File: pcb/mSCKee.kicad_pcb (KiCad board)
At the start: 2 copper layers, 184 parts, among them IC1 PCA9956BTWY, IC2 PCA9956BTWY, J1 USB_C_Receptacle_USB2.0_14P, J2 4P4C, J3 4P4C, SW1 SW_Push_45deg, SW10 SW_Push_45deg, SW11 SW_Push_45deg, SW12 SW_Push_45deg, SW13 SW_Push_45deg, SW14 SW_Push_45deg, SW15 SW_Push_45deg, SW16 SW_Push_45deg, SW17 SW_Push_45deg, SW18 SW_Push_45deg, SW19 SW_Push, SW2 SW_Push_45deg, SW20 SW_Push, SW21 SW_SP3T, SW22 SW_Push_45deg, SW23 SW_Push_45deg, SW24 SW_Push_45deg, SW25 SW_Push_45deg, SW26 SW_Push_45deg, SW27 SW_Push_45deg, SW28 SW_Push_45deg, SW29 SW_Push_45deg, SW3 SW_Push_45deg, SW30 SW_Push_45deg, SW31 SW_Push_45deg, SW32 SW_Push_45deg, SW33 SW_Push_45deg, SW34 SW_Push_45deg, SW35 SW_Push_45deg, SW36 SW_Push_45deg, SW37 SW_Push_45deg, SW38 SW_Push_45deg, SW39 SW_Push_45deg, SW4 SW_Push_45deg, SW5 SW_Push_45deg, SW6 SW_Push_45deg, SW7 SW_Push_45deg, SW8 SW_Push_45deg, SW9 SW_Push_45deg, U1 W25Q128JVSIQ, U2 RP2040, U3 NCP1117LPST33T3G, U4 OPT3001DNPR, U5 NCP1117LPST33T3G, U6 MCP23017T-E/ML, U7 OPT3001DNPR, Y1 ABM8-272-T3

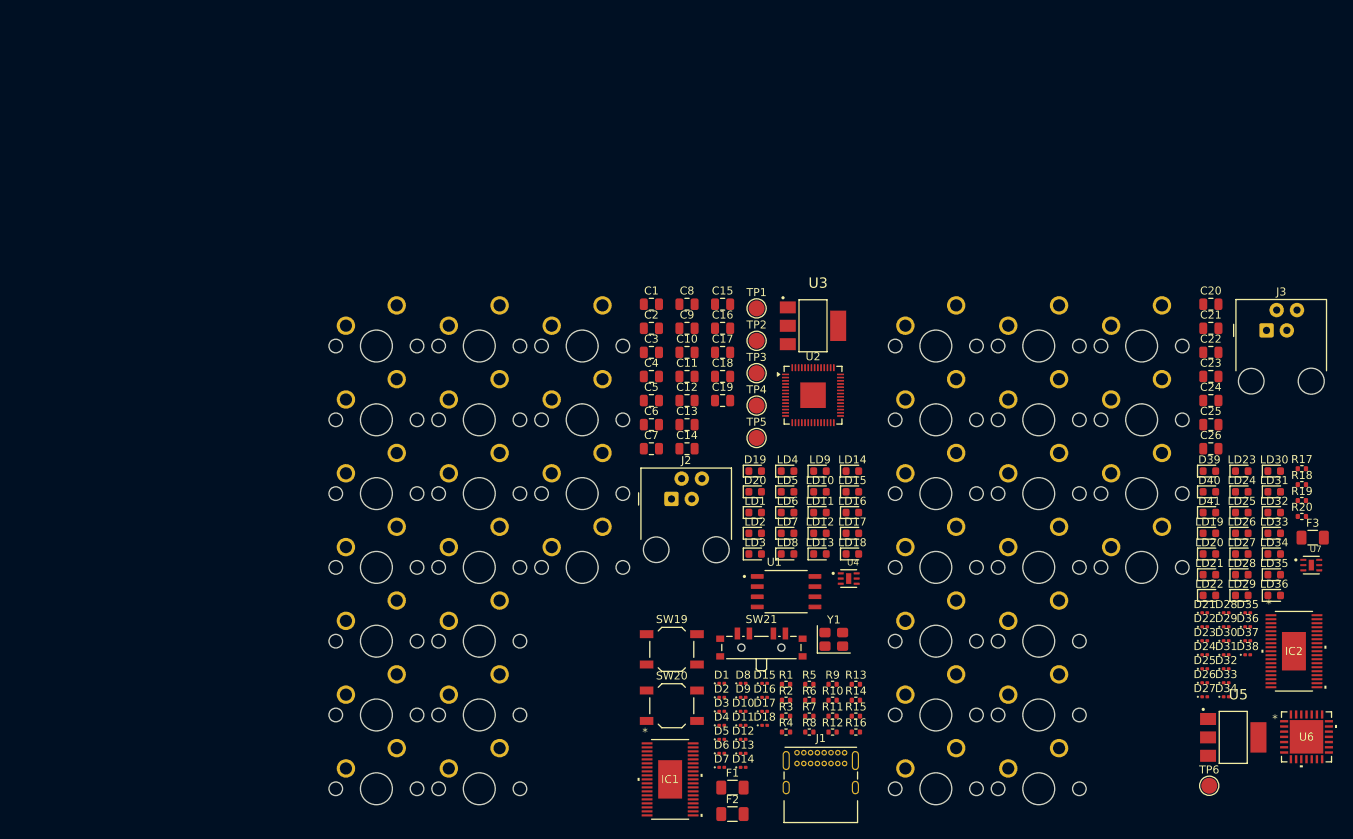
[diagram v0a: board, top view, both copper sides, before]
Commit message: fix: Proper USB-C receptacle symbol
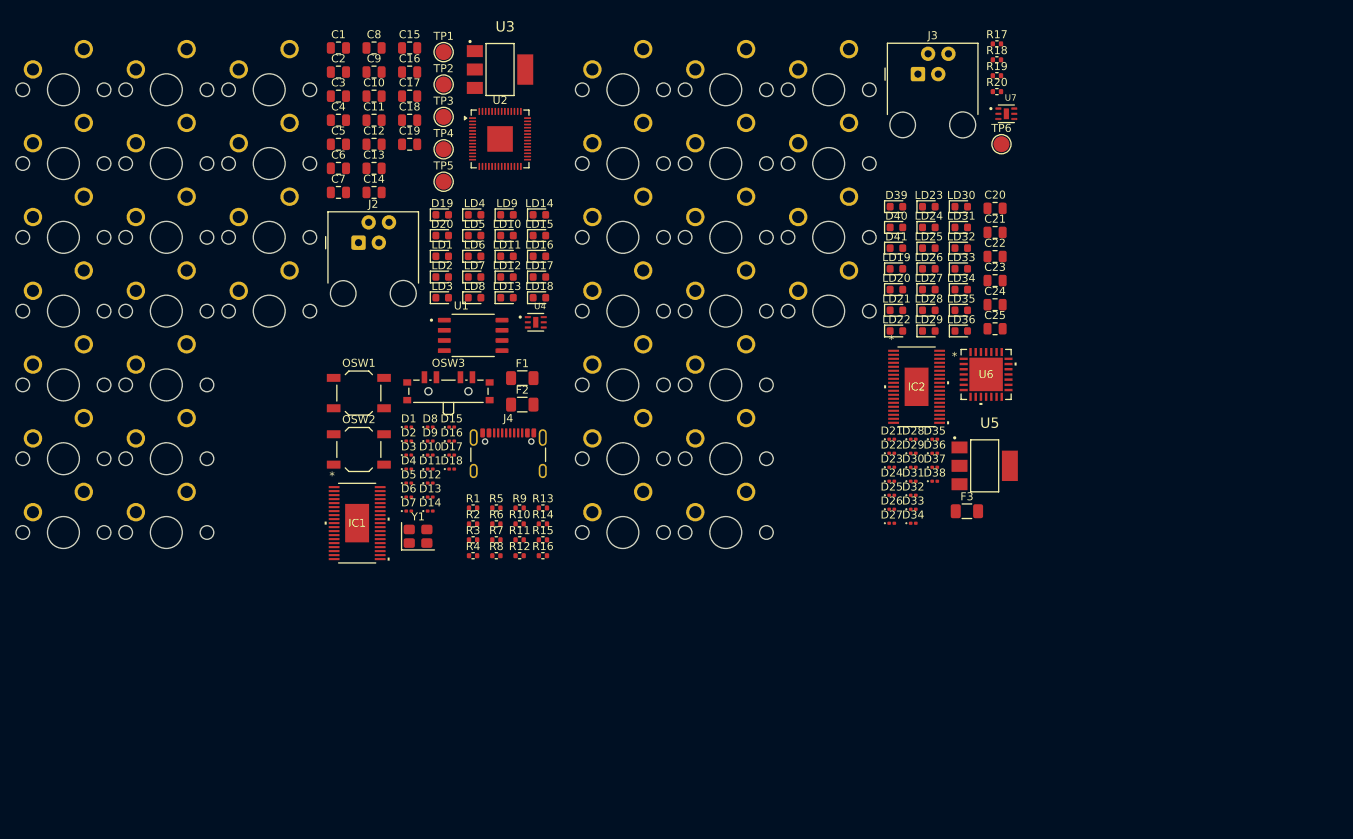
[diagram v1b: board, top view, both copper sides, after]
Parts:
- removed C26: 10u, Capacitor_SMD:C_0805_2012Metric
- removed J1: USB_C_Receptacle_USB2.0_14P, Connector_USB:USB_C_Receptacle_GCT_USB4085
- removed SW37, SW38, SW39: SW_Push_45deg, ai03-MX_V2:MX-Solderable-1U
- added J4: USB_C_Receptacle_USB2.0_16P, Connector_USB:USB_C_Receptacle_GCT_USB4105-xx-A_16P_TopMnt_Horizontal, F.Cu at (194.8, 137.9)
- added OSW1: SW_Push, Button_Switch_SMD:SW_SPST_TL3342, F.Cu at (176.1, 129.2)
- added OSW2: SW_Push, Button_Switch_SMD:SW_SPST_TL3342, F.Cu at (176.1, 136.3)
- added OSW3: SW_SP3T, Button_Switch_SMD:SW_SP3T_PCM13, F.Cu at (187.3, 128.7)
- C20: value 20u -> 10u
- C22: value 10u -> 100n
- C25: value 100n -> 10u
- R13: value R -> 10k
- R15: value 10k -> R
- SW19, SW20: value SW_Push -> SW_Push_45deg; footprint Button_Switch_SMD:SW_SPST_TL3342 -> ai03-MX_V2:MX-Solderable-1U
- SW21: value SW_SP3T -> SW_Push_45deg; footprint Button_Switch_SMD:SW_SP3T_PCM13 -> ai03-MX_V2:MX-Solderable-1U
- moved TP6 84.3 mm to (256.4, 98.1)
- moved SW27 73.8 mm to (222.0, 100.5)
- moved SW26 73.8 mm to (222.0, 91.3)
- moved SW28 73.8 mm to (222.0, 109.8)
- moved SW34 73.8 mm to (234.8, 100.5)
- moved SW33 73.8 mm to (234.8, 91.3)
- moved SW35 73.8 mm to (234.8, 109.8)
- moved SW19 70.2 mm to (209.1, 91.3)
- moved U7 68.1 mm to (257.0, 94.3)
- moved SW20 68.0 mm to (209.1, 100.5)
- moved R18 65.4 mm to (255.8, 87.6)
- moved R17 65.4 mm to (255.8, 85.6)
- moved R20 65.4 mm to (255.8, 91.5)
- moved R19 65.4 mm to (255.8, 89.6)
- moved U6 60.5 mm to (254.5, 126.9)
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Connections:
- net GPIO0 renamed I2C_D_R
- net GPIO1 renamed I2C_CLK_R
- net GPIO2 renamed I2C_D
- net GPIO3 renamed I2C_CLK
- net GPIO5 renamed STATUS2
- C21 pad 1: +5V_R -> +3V3_R
- C22 pad 1: +3V3_R -> unconnected-(C22-Pad1)
- C22 pad 2: unconnected-(C22-Pad2) -> +3V3_R
- C24 pad 1: unconnected-(C24-Pad1) -> +3V3_R
- C24 pad 2: +3V3_R -> unconnected-(C24-Pad2)
- C25 pad 1: +3V3_R -> +5V_R
- R13 pad 1: GPIO4 -> OE_ENABLE
- R13 pad 2: Net-(D19-A) -> +3V3
- R14 pad 1: OE_ENABLE -> +3V3
- R14 pad 2: +3V3 -> Net-(IC1-RESET)
- R15 pad 1: +3V3 -> STATUS1
- R15 pad 2: Net-(IC1-RESET) -> Net-(D19-A)
- R9 pad 2: Net-(R9-Pad2) -> Net-(OSW1-Pad2)
- SW19 pad 1: GND -> COL1R
- SW19 pad 2: Net-(R9-Pad2) -> Net-(D21-A)
- SW20 pad 1: GND -> COL2R
- SW20 pad 2: Net-(U2-RUN) -> Net-(D22-A)
- SW21 pad 1: GPIO6 -> COL3R
- SW21 pad 2: GPIO7 -> Net-(D23-A)
- SW22 pad 1: COL1R -> COL4R
- SW22 pad 2: Net-(D21-A) -> Net-(D24-A)
- SW23 pad 1: COL2R -> COL5R
- SW23 pad 2: Net-(D22-A) -> Net-(D25-A)
- SW24 pad 1: COL3R -> COL6R
- SW24 pad 2: Net-(D23-A) -> Net-(D26-A)
- SW25 pad 1: COL4R -> COL1R
- SW25 pad 2: Net-(D24-A) -> Net-(D27-A)
- SW26 pad 1: COL5R -> COL2R
- SW26 pad 2: Net-(D25-A) -> Net-(D28-A)
- SW27 pad 1: COL6R -> COL3R
- SW27 pad 2: Net-(D26-A) -> Net-(D29-A)
- SW28 pad 1: COL1R -> COL4R
- SW28 pad 2: Net-(D27-A) -> Net-(D30-A)
- SW29 pad 1: COL2R -> COL5R
- SW29 pad 2: Net-(D28-A) -> Net-(D31-A)
- SW30 pad 1: COL3R -> COL6R
- SW30 pad 2: Net-(D29-A) -> Net-(D32-A)
- SW31 pad 1: COL4R -> COL1R
- SW31 pad 2: Net-(D30-A) -> Net-(D33-A)
- SW32 pad 1: COL5R -> COL2R
- SW32 pad 2: Net-(D31-A) -> Net-(D34-A)
- SW33 pad 1: COL6R -> COL3R
- SW33 pad 2: Net-(D32-A) -> Net-(D35-A)
- SW34 pad 1: COL1R -> COL4R
- SW34 pad 2: Net-(D33-A) -> Net-(D36-A)
- SW35 pad 1: COL2R -> COL5R
- SW35 pad 2: Net-(D34-A) -> Net-(D37-A)
- SW36 pad 1: COL3R -> COL6R
- SW36 pad 2: Net-(D35-A) -> Net-(D38-A)
- U2 pad 11: GPIO8 -> BL_DIM_3
- U2 pad 6: GPIO4 -> STATUS1
- U2 pad 8: GPIO6 -> BL_DIM_1
- U2 pad 9: GPIO7 -> BL_DIM_2

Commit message: fix: Fix thumb cluster key splay & Correctly align keys to outline in PCB layout
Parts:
- D1, D10, D11, D12, D13, D14, D15, D16, D17, D18, D2, D21, D22, D23, D24, D25, D26, D27, D28, D29, D3, D30, D31, D32, D33, D34, D35, D36, D37, D38, D4, D5, D6, D7, D8, D9: moved to B.Cu
- moved SW10 182.3 mm to (333.8, 96.2)
- moved LD29 163.8 mm to (83.8, 131.1)
- moved SW8 160.8 mm to (312.9, 90.5)
- moved LD19 159.5 mm to (83.8, 111.1)
- moved D10 158.2 mm to (338.9, 100.2), turned to 90 degrees
- moved D31 156.5 mm to (88.9, 140.2), turned to 90 degrees
- moved D21 154.5 mm to (88.9, 120.2), turned to 90 degrees
- moved SW2 154.1 mm to (291.9, 80.0)
- moved SW18 148.2 mm to (312.9, 110.5)
- moved LD27 142.9 mm to (104.8, 125.4)
- moved SW12 142.7 mm to (291.9, 100.0)
- moved LD10 140.4 mm to (333.8, 91.1)
- moved SW29 139.2 mm to (83.8, 136.2)
- moved D8 138.5 mm to (317.9, 94.5), turned to 90 degrees
- moved SW4 136.4 mm to (271.0, 83.8)
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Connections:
- D1 pad 1: ROW1 -> ROW0
- D10 pad 1: ROW2 -> ROW1
- D11 pad 1: ROW2 -> ROW1
- D12 pad 1: ROW2 -> ROW1
- D13 pad 1: ROW3 -> ROW2
- D14 pad 1: ROW3 -> ROW2
- D15 pad 1: ROW3 -> ROW2
- D16 pad 1: ROW3 -> ROW2
- D17 pad 1: ROW3 -> ROW2
- D18 pad 1: ROW3 -> ROW2
- D2 pad 1: ROW1 -> ROW0
- D21 pad 1: ROW1R -> ROW0
- D22 pad 1: ROW1R -> ROW0
- D23 pad 1: ROW1R -> ROW0
- D24 pad 1: ROW1R -> ROW0
- D25 pad 1: ROW1R -> ROW0
- D26 pad 1: ROW1R -> ROW0
- D27 pad 1: ROW2R -> ROW1
- D28 pad 1: ROW2R -> ROW1
- D29 pad 1: ROW2R -> ROW1
- D3 pad 1: ROW1 -> ROW0
- D30 pad 1: ROW2R -> ROW1
- D31 pad 1: ROW2R -> ROW1
- D32 pad 1: ROW2R -> ROW1
- D33 pad 1: ROW3R -> ROW2
- D34 pad 1: ROW3R -> ROW2
- D35 pad 1: ROW3R -> ROW2
- D36 pad 1: ROW3R -> ROW2
- D37 pad 1: ROW3R -> ROW2
- D38 pad 1: ROW3R -> ROW2
- D4 pad 1: ROW1 -> ROW0
- D5 pad 1: ROW1 -> ROW0
- D6 pad 1: ROW1 -> ROW0
- D7 pad 1: ROW2 -> ROW1
- D8 pad 1: ROW2 -> ROW1
- D9 pad 1: ROW2 -> ROW1
- SW1 pad 1: COL1 -> COL0
- SW10 pad 1: COL4 -> COL3
- SW11 pad 1: COL5 -> COL4
- SW12 pad 1: COL6 -> COL5
- SW13 pad 1: COL1 -> COL0
- SW14 pad 1: COL2 -> COL1
- SW15 pad 1: COL3 -> COL2
- SW16 pad 1: COL4 -> COL3
- SW17 pad 1: COL5 -> COL4
- SW18 pad 1: COL6 -> COL5
- SW19 pad 1: COL1R -> COL6
- SW2 pad 1: COL2 -> COL1
- SW20 pad 1: COL2R -> COL7
- SW21 pad 1: COL3R -> COL8
- SW22 pad 1: COL4R -> COL9
- SW23 pad 1: COL5R -> COL10
- SW24 pad 1: COL6R -> COL11
- SW25 pad 1: COL1R -> COL6
- SW26 pad 1: COL2R -> COL7
- SW27 pad 1: COL3R -> COL8
- SW28 pad 1: COL4R -> COL9
- SW29 pad 1: COL5R -> COL10
- SW3 pad 1: COL3 -> COL2
- SW30 pad 1: COL6R -> COL11
- SW31 pad 1: COL1R -> COL6
- SW32 pad 1: COL2R -> COL7
- SW33 pad 1: COL3R -> COL8
- SW34 pad 1: COL4R -> COL9
- SW35 pad 1: COL5R -> COL10
- SW36 pad 1: COL6R -> COL11
- SW4 pad 1: COL4 -> COL3
- SW5 pad 1: COL5 -> COL4
- SW6 pad 1: COL6 -> COL5
- SW7 pad 1: COL1 -> COL0
- SW8 pad 1: COL2 -> COL1
- SW9 pad 1: COL3 -> COL2
- U2 pad 12: ROW1 -> ROW0
- U2 pad 13: ROW2 -> ROW1
- U2 pad 14: ROW3 -> ROW2
- U2 pad 15: COL1 -> COL0
- U2 pad 16: COL2 -> COL1
- U2 pad 17: COL3 -> COL2
- U2 pad 18: COL4 -> COL3
- U2 pad 27: COL5 -> COL4
- U2 pad 28: COL6 -> COL5
- U6 pad 17: ROW1R -> ROW2
- U6 pad 18: ROW2R -> ROW1
- U6 pad 19: ROW3R -> ROW0
- U6 pad 20: COL1R -> COL11
- U6 pad 21: COL2R -> COL10
- U6 pad 22: COL3R -> COL9
- U6 pad 23: COL4R -> COL8
- U6 pad 24: COL5R -> COL7
- U6 pad 25: COL6R -> COL6
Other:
- board outline added: 275.5 x 124.6 mm

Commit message: chore(for future reference): Properly lay out keys, keep components unrouted
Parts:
- moved C1 149.6 mm to (45.2, 224.1)
- moved C2 149.6 mm to (45.2, 227.1)
- moved C3 149.6 mm to (45.2, 230.1)
- moved C4 149.6 mm to (45.2, 233.1)
- moved C5 149.6 mm to (45.2, 236.2)
- moved C6 149.6 mm to (45.2, 239.2)
- moved C7 149.6 mm to (45.2, 242.2)
- moved D19 149.6 mm to (58.2, 245.0)
- moved D20 149.6 mm to (58.2, 247.6)
- moved J4 149.6 mm to (66.4, 275.9)
- moved OSW3 149.6 mm to (58.9, 266.7)
- moved R13 149.6 mm to (70.8, 281.6)
- moved R14 149.6 mm to (70.8, 283.6)
- moved R15 149.6 mm to (70.8, 285.6)
- moved R16 149.6 mm to (70.8, 287.6)
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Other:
- board size 275.5 x 124.6 mm -> 275.3 x 124.4 mm
- copper layers 2 -> 4
- rule pad_to_mask_clearance: 0.05 -> 0

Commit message: fix(broken): Reroute USB
TODO:
- Fix 0402 imperial and metric confusion
- Fix DRC errors (are holes of claws of USB-C and ethernet big enough to manufacture?)
- Proper decoupling cap distribution between pins
- Manage the +1.1V and +3.3V situation (maybe create +1.1V net)
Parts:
- added ?: , , F.Cu at (184.3, 119.7)
- added ?: , , F.Cu at (184.3, 117.1)
- added ?: , , F.Cu at (183.1, 119.7)
- added ?: , , F.Cu at (185.6, 118.4)
- added ?: , , F.Cu at (184.3, 118.4)
- added ?: , , F.Cu at (183.1, 117.1)
- added ?: , , F.Cu at (185.6, 117.1)
- added ?: , , F.Cu at (185.6, 119.7)
- added ?: , , F.Cu at (183.1, 118.4)
- added C8: 1u, Capacitor_SMD:C_0402_1005Metric, F.Cu at (338.5, 0.58)
- C10, C11: footprint Capacitor_SMD:C_0805_2012Metric -> Capacitor_SMD:C_01005_0402Metric
- C8, C9: footprint Capacitor_SMD:C_0805_2012Metric -> Capacitor_SMD:C_0402_1005Metric
- moved R8 237.3 mm to (188.8, 85.2), turned to 90 degrees
- moved R7 234.0 mm to (185.2, 84.9), turned to 90 degrees
- moved J4 231.8 mm to (187.0, 78.0), turned to 180 degrees
- moved F1 217.5 mm to (191.5, 86.2), turned to -90 degrees
- moved F2 216.0 mm to (194.5, 93.5), turned to -90 degrees
- moved R2 211.8 mm to (185.3, 111.4), turned to -90 degrees
- moved C13 210.3 mm to (194.2, 86.5), turned to 90 degrees
- moved R1 209.5 mm to (184.2, 111.4), turned to -90 degrees
- moved J2 202.7 mm to (190.2, 104.2), turned to 90 degrees
- moved U4 197.7 mm to (125.0, 68.5)
- moved TP2 192.1 mm to (191.5, 90.2)
- moved C11 182.7 mm to (186.2, 111.8), turned to 90 degrees
- moved C10 180.5 mm to (187.7, 113.9)
- moved C8 179.2 mm to (189.0, 111.3), turned to -90 degrees
- moved U3 174.3 mm to (181.1, 96.5), turned to -90 degrees
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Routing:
- net /master_side/USB_D+: track 0.00 -> 60.3 mm
- net /master_side/USB_D-: track 0.00 -> 59.2 mm, vias 0 -> 2
- net +5V: track 0.00 -> 25.0 mm, vias 0 -> 2
- net Net-(U2-VREG_VOUT): track 0.00 -> 22.4 mm, vias 0 -> 3
- net Net-(F2-Pad2): track 0.00 -> 11.1 mm, vias 0 -> 1
- net Net-(F1-Pad1): track 0.00 -> 10.9 mm, vias 0 -> 2
- net +3V3: track 0.00 -> 7.74 mm, vias 0 -> 6
- net Net-(U2-USB_DP): track 0.00 -> 3.54 mm
- net Net-(U2-USB_DM): track 0.00 -> 3.35 mm
- net Net-(J4-CC1): track 0.00 -> 3.17 mm
- net Net-(J4-CC2): track 0.00 -> 2.71 mm
- net GND: track 0.00 -> 1.22 mm, vias 0 -> 16
- added copper zone on In2.Cu, net +3V3
- added copper zone on In1.Cu, net GND
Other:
- outline, holes or cut-outs redrawn

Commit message: feat: Improve layout & route crystal and flash
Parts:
- removed the C8 at (189.0, 111.3)
- removed the C8 at (338.5, 0.58)
- added C8: 100n, Capacitor_SMD:C_0402_1005Metric, F.Cu at (183.7, 112.1)
- C1, C2, C3, C4, C5, C6, C7: footprint Capacitor_SMD:C_0805_2012Metric -> Capacitor_SMD:C_0402_1005Metric
- C10, C11: footprint Capacitor_SMD:C_01005_0402Metric -> Capacitor_SMD:C_0402_1005Metric
- R15, R16: footprint Resistor_SMD:R_0402_1005Metric -> Resistor_SMD:R_0201_0603Metric
- R3, R4: moved to B.Cu
- moved R14 316.3 mm to (246.9, 20.8)
- moved R13 316.3 mm to (246.9, 18.9)
- moved IC1 310.5 mm to (214.8, 21.9)
- moved R12 307.3 mm to (224.2, 23.0)
- moved C19 277.1 mm to (231.2, 23.0)
- moved C17 276.8 mm to (231.4, 17.6)
- moved R5 242.2 mm to (212.5, 89.5)
- moved R6 241.7 mm to (212.4, 92.1)
- moved R3 222.2 mm to (183.9, 99.8), turned to -90 degrees
- moved R4 220.9 mm to (183.5, 103.1), turned to 90 degrees
- moved OSW1 213.4 mm to (193.9, 111.7)
- moved R16 211.4 mm to (197.1, 118.2)
- moved R15 210.4 mm to (197.1, 117.3)
- moved R9 209.2 mm to (186.4, 109.2)
- moved R11 203.9 mm to (191.1, 123.2), turned to -90 degrees
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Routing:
- net +3V3: track 7.74 -> 38.9 mm, vias 6 -> 23
- net I2C_CLK_R: track 0.00 -> 24.8 mm, vias 0 -> 2
- net Net-(U2-RUN): track 0.00 -> 24.0 mm
- net I2C_D_R: track 0.00 -> 23.7 mm, vias 0 -> 1
- net STATUS1: track 0.00 -> 22.2 mm, vias 0 -> 2
- net STATUS2: track 0.00 -> 21.4 mm, vias 0 -> 2
- net /master_side/QSPI_SD2: track 0.00 -> 13.1 mm, vias 0 -> 2
- net Net-(OSW1-Pad2): track 0.00 -> 12.8 mm
- net /master_side/QSPI_SD1: track 0.00 -> 11.6 mm, vias 0 -> 2
- net /master_side/XIN: track 0.00 -> 8.73 mm, vias 0 -> 2
- net Net-(U2-SWD): track 0.00 -> 7.31 mm
- net /master_side/QSPI_SD0: track 0.00 -> 6.93 mm
- net /master_side/QSPI_SCLK: track 0.00 -> 5.94 mm
- net GND: track 1.22 -> 6.96 mm, vias 16 -> 40
- net /master_side/QSPI_SD3: track 0.00 -> 5.04 mm
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
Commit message: feat: Add NC flags to both side schematics
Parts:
- C12: footprint Capacitor_SMD:C_0805_2012Metric -> Capacitor_SMD:C_0402_1005Metric
- R9: moved to B.Cu
- moved IC1 134.8 mm to (80.9, 36.7)
- moved IC2 88.3 mm to (307.6, 201.8)
- moved C17 54.9 mm to (176.6, 18.5)
- moved C19 54.9 mm to (176.3, 23.9)
- moved R12 54.9 mm to (169.4, 23.9)
- moved R13 54.9 mm to (192.0, 19.7)
- moved R14 54.9 mm to (192.0, 21.7)
- moved C12 0.97 mm to (188.4, 109.2), turned to 180 degrees
- turned R9 to 180 degrees
- gave numbers to parts that had none: 9
- renumbered D15 to D10, D31 to D11, D29 to D12, D23 to D13, D25 to D14, D27 to D15, D33 to D16, D35 to D17, D37 to D18, D6 to D19, D7 to D2, D4 to D20, D2 to D21, D8 to D22, D10 to D23, D16 to D24, D14 to D25, D12 to D26, D18 to D27, D22 to D28, D28 to D29, D1 to D3, D26 to D30, D24 to D31, D30 to D32, D32 to D33, D36 to D34, D34 to D35, D38 to D36, D3 to D4, D9 to D6, D21 to D6, D17 to D7, D11 to D8, D13 to D9, LD9 to LD1, LD15 to LD10, LD29 to LD11, LD27 to LD12, LD21 to LD13, LD23 to LD14, LD25 to LD15, LD31 to LD16, LD33 to LD17, LD35 to LD18, LD6 to LD19, LD7 to LD2, LD4 to LD20, LD2 to LD21, LD8 to LD22, LD10 to LD23, LD16 to LD24, LD14 to LD25, LD12 to LD26, LD18 to LD27, LD20 to LD28, LD26 to LD29, LD1 to LD3, LD24 to LD30, LD22 to LD31, LD28 to LD32, LD30 to LD33, LD32 to LD35, LD3 to LD4, LD19 to LD6, LD17 to LD7, LD11 to LD8, LD13 to LD9, SW9 to SW1, SW15 to SW10, SW29 to SW11, SW27 to SW12, SW21 to SW13, SW23 to SW14, SW25 to SW15, SW31 to SW16, SW33 to SW17, SW35 to SW18, SW6 to SW19, SW7 to SW2, SW4 to SW20, SW2 to SW21, SW8 to SW22, SW10 to SW23, SW16 to SW24, SW14 to SW25, SW12 to SW26, SW18 to SW27, SW20 to SW28, SW26 to SW29, SW1 to SW3, SW24 to SW30, SW22 to SW31, SW28 to SW32, SW30 to SW33, SW32 to SW35, SW3 to SW4, SW19 to SW6, SW17 to SW7, SW11 to SW8, SW13 to SW9
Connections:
- D10 pad 1: ROW2 -> ROW1
- D11 pad 1: ROW1 -> ROW2
- D12 pad 1: ROW1 -> ROW2
- D13 pad 1: ROW0 -> ROW2
- D14 pad 1: ROW0 -> ROW2
- D15 pad 1: ROW1 -> ROW2
- D2 pad 1: ROW1 -> ROW0
- D22 pad 1: ROW1 -> ROW0
- D23 pad 1: ROW1 -> ROW0
- D24 pad 1: ROW2 -> ROW1
- D25 pad 1: ROW2 -> ROW1
- D27 pad 1: ROW2 -> ROW1
- D28 pad 1: ROW0 -> ROW1
- D29 pad 1: ROW1 -> ROW2
- D30 pad 1: ROW0 -> ROW2
- D31 pad 1: ROW0 -> ROW2
- D32 pad 1: ROW1 -> ROW2
- D33 pad 1: ROW1 -> ROW2
- D6 pad 1: ROW1 -> ROW0
- D6 pad 1: ROW0 -> ROW1
- D7 pad 1: ROW2 -> ROW1
- D9 pad 1: ROW2 -> ROW1
- SW1 pad 1: COL2 -> COL0
- SW10 pad 1: COL2 -> COL4
- SW11 pad 1: COL10 -> COL0
- SW12 pad 1: COL8 -> COL1
- SW13 pad 1: COL8 -> COL2
- SW14 pad 1: COL10 -> COL3
- SW15 pad 1: COL6 -> COL4
- SW17 pad 1: COL8 -> COL6
- SW18 pad 1: COL10 -> COL6
- SW19 pad 1: COL5 -> COL7
- SW2 pad 1: COL0 -> COL1
- SW20 pad 1: COL3 -> COL8
- SW21 pad 1: COL1 -> COL9
- SW22 pad 1: COL1 -> COL10
- SW23 pad 1: COL3 -> COL11
- SW24 pad 1: COL3 -> COL7
- SW25 pad 1: COL1 -> COL8
- SW26 pad 1: COL5 -> COL9
- SW27 pad 1: COL5 -> COL10
- SW28 pad 1: COL7 -> COL11
- SW3 pad 1: COL0 -> COL2
- SW30 pad 1: COL11 -> COL8
- SW32 pad 1: COL9 -> COL10
- SW34 pad 1: COL9 -> COL7
- SW36 pad 1: COL11 -> COL7
- SW4 pad 1: COL2 -> COL3
- SW6 pad 1: COL6 -> COL0
- SW7 pad 1: COL4 -> COL1
- SW8 pad 1: COL4 -> COL2
- SW9 pad 1: COL0 -> COL3
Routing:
- net +3V3: track 38.9 -> 37.1 mm, vias 23 -> 20
- net Net-(OSW1-Pad2): track 12.8 -> 13.5 mm, vias 0 -> 1
